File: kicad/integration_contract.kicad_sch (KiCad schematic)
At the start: 0 parts

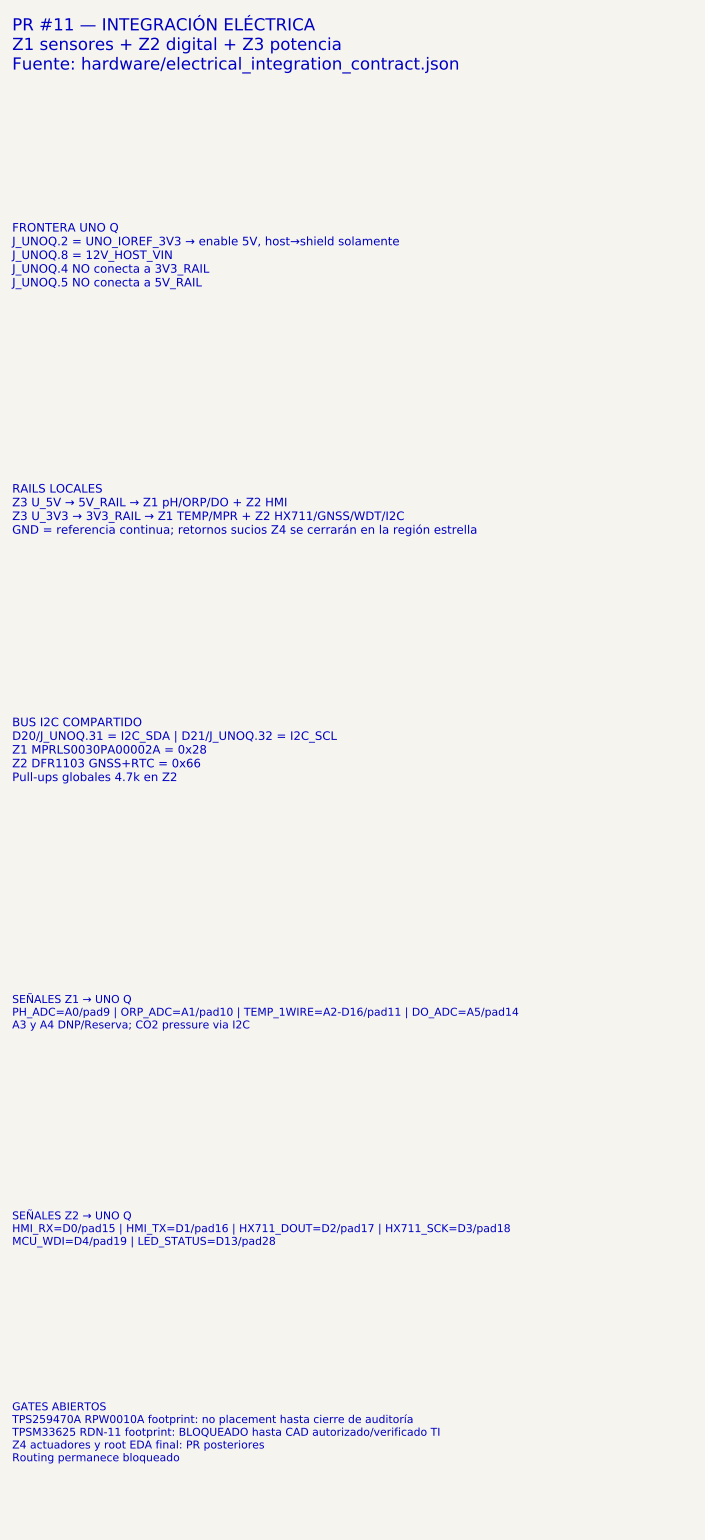
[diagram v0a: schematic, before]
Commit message: actuadores: congelar Z4 protegido y diagnosticable para Insight (#12)
Sustituye etapas legacy por DRV8242H-Q1, TPS1HC120C-Q1 y PhotoMOS AQY212EHAX; añade telemetría de bomba en A4, diagnóstico común D10, SELV/no-mains para chiller y gates Z4 con 10/10 checks verdes.
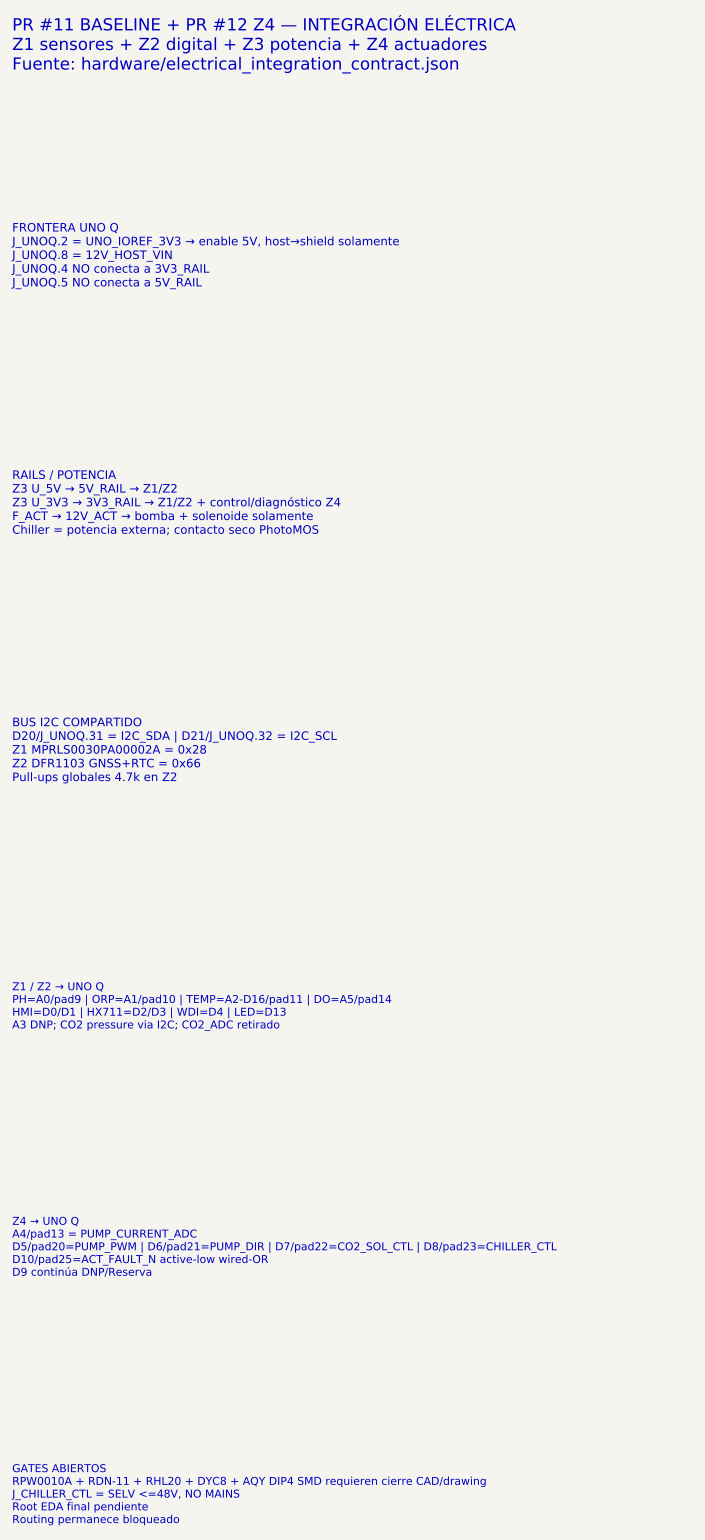
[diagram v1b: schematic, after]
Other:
- note added: "GATES ABIERTOS RPW0010A + RDN-11 + RHL20 + DYC8 + AQY DIP4 SMD requieren cierre CAD/drawing J_CHILLER_CTL = SELV <=48V, NO MAINS Root EDA final pendiente Routing permanece bloqueado"
- note added: "PR #11 BASELINE + PR #12 Z4 — INTEGRACIÓN ELÉCTRICA Z1 sensores + Z2 digital + Z3 potencia + Z4 actuadores Fuente: hardware/electrical_integration_contract.json"
- note added: "RAILS / POTENCIA Z3 U_5V → 5V_RAIL → Z1/Z2 Z3 U_3V3 → 3V3_RAIL → Z1/Z2 + control/diagnóstico Z4 F_ACT → 12V_ACT → bomba + solenoide solamente Chiller = potencia externa; contacto seco PhotoMOS"
- note added: "Z1 / Z2 → UNO Q PH=A0/pad9 | ORP=A1/pad10 | TEMP=A2-D16/pad11 | DO=A5/pad14 HMI=D0/D1 | HX711=D2/D3 | WDI=D4 | LED=D13 A3 DNP; CO2 pressure via I2C; CO2_ADC retirado"
- note added: "Z4 → UNO Q A4/pad13 = PUMP_CURRENT_ADC D5/pad20=PUMP_PWM | D6/pad21=PUMP_DIR | D7/pad22=CO2_SOL_CTL | D8/pad23=CHILLER_CTL D10/pad25=ACT_FAULT_N active-low wired-OR D9 continúa DNP/Reserva"
- note removed: "GATES ABIERTOS TPS259470A RPW0010A footprint: no placement hasta cierre de auditoría TPSM33625 RDN-11 footprint: BLOQUEADO hasta CAD autorizado/verificado TI Z4 actuadores y root EDA final: PR posteriores Routing permanece bloqueado"
- note removed: "PR #11 — INTEGRACIÓN ELÉCTRICA Z1 sensores + Z2 digital + Z3 potencia Fuente: hardware/electrical_integration_contract.json"
- note removed: "RAILS LOCALES Z3 U_5V → 5V_RAIL → Z1 pH/ORP/DO + Z2 HMI Z3 U_3V3 → 3V3_RAIL → Z1 TEMP/MPR + Z2 HX711/GNSS/WDT/I2C GND = referencia continua; retornos sucios Z4 se cerrarán en la región estrella"
- note removed: "SEÑALES Z1 → UNO Q PH_ADC=A0/pad9 | ORP_ADC=A1/pad10 | TEMP_1WIRE=A2-D16/pad11 | DO_ADC=A5/pad14 A3 y A4 DNP/Reserva; CO2 pressure via I2C"
- note removed: "SEÑALES Z2 → UNO Q HMI_RX=D0/pad15 | HMI_TX=D1/pad16 | HX711_DOUT=D2/pad17 | HX711_SCK=D3/pad18 MCU_WDI=D4/pad19 | LED_STATUS=D13/pad28"
- title: NFB Insight PCBA v2 — Integración eléctrica Z1 + Z2 + Potencia -> NFB Insight PCBA v2 — Integración eléctrica Z1 + Z2 + Z3 + Z4
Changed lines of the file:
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@@
 (kicad_sch
   (version 20250114)
-  (generator "nfb_pr11_integration_contract")
+  (generator "nfb_pr12_integration_contract")
   (generator_version "1.0")
   (paper "A3")
   (title_block
-    (title "NFB Insight PCBA v2 — Integración eléctrica Z1 + Z2 + Potencia")
+    (title "NFB Insight PCBA v2 — Integración eléctrica Z1 + Z2 + Z3 + Z4")
     (date "2026-08-12")
-    (rev "0.11.0")
+    (rev "0.12.0")
     (company "Cafelium SRL / Nebula Ecosystem")
-    (comment 1 "PR #11 — contrato de integración, no placement/routing")
+    (comment 1 "PR #11 baseline + extensión PR #12 Z4; no placement/routing")
     (comment 2 "Fuente de verdad: hardware/electrical_integration_contract.json")
-    (comment 3 "Z4 actuadores queda fuera de alcance")
-    (comment 4 "Footprints críticos abiertos bloquean placement de potencia")
+    (comment 3 "Z4 actuadores integrado contractualmente")
+    (comment 4 "Footprints críticos abiertos bloquean placement")
   )
-  (text "PR #11 — INTEGRACIÓN ELÉCTRICA\nZ1 sensores + Z2 digital + Z3 potencia\nFuente: hardware/electrical_integration_contract.json"
+  (text "PR #11 BASELINE + PR #12 Z4 — INTEGRACIÓN ELÉCTRICA\nZ1 sensores + Z2 digital + Z3 potencia + Z4 actuadores\nFuente: hardware/electrical_integration_contract.json"
     (exclude_from_sim no)
     (at 30.48 30.48 0)
@@
     (effects (font (size 1.4 1.4)) (justify left bottom))
   )
-  (text "RAILS LOCALES\nZ3 U_5V → 5V_RAIL → Z1 pH/ORP/DO + Z2 HMI\nZ3 U_3V3 → 3V3_RAIL → Z1 TEMP/MPR + Z2 HX711/GNSS/WDT/I2C\nGND = referencia continua; retornos sucios Z4 se cerrarán en la región estrella"
+  (text "RAILS / POTENCIA\nZ3 U_5V → 5V_RAIL → Z1/Z2\nZ3 U_3V3 → 3V3_RAIL → Z1/Z2 + control/diagnóstico Z4\nF_ACT → 12V_ACT → bomba + solenoide solamente\nChiller = potencia externa; contacto seco PhotoMOS"
     (exclude_from_sim no)
     (at 30.48 106.68 0)
@@
     (effects (font (size 1.4 1.4)) (justify left bottom))
   )
-  (text "SEÑALES Z1 → UNO Q\nPH_ADC=A0/pad9 | ORP_ADC=A1/pad10 | TEMP_1WIRE=A2-D16/pad11 | DO_ADC=A5/pad14\nA3 y A4 DNP/Reserva; CO2 pressure via I2C"
+  (text "Z1 / Z2 → UNO Q\nPH=A0/pad9 | ORP=A1/pad10 | TEMP=A2-D16/pad11 | DO=A5/pad14\nHMI=D0/D1 | HX711=D2/D3 | WDI=D4 | LED=D13\nA3 DNP; CO2 pressure via I2C; CO2_ADC retirado"
     (exclude_from_sim no)
     (at 30.48 187.96 0)
     (effects (font (size 1.3 1.3)) (justify left bottom))
   )
-  (text "SEÑALES Z2 → UNO Q\nHMI_RX=D0/pad15 | HMI_TX=D1/pad16 | HX711_DOUT=D2/pad17 | HX711_SCK=D3/pad18\nMCU_WDI=D4/pad19 | LED_STATUS=D13/pad28"
+  (text "Z4 → UNO Q\nA4/pad13 = PUMP_CURRENT_ADC\nD5/pad20=PUMP_PWM | D6/pad21=PUMP_DIR | D7/pad22=CO2_SOL_CTL | D8/pad23=CHILLER_CTL\nD10/pad25=ACT_FAULT_N active-low wired-OR\nD9 continúa DNP/Reserva"
     (exclude_from_sim no)
-    (at 30.48 223.52 0)
+    (at 30.48 228.6 0)
     (effects (font (size 1.3 1.3)) (justify left bottom))
   )
-  (text "GATES ABIERTOS\nTPS259470A RPW0010A footprint: no placement hasta cierre de auditoría\nTPSM33625 RDN-11 footprint: BLOQUEADO hasta CAD autorizado/verificado TI\nZ4 actuadores y root EDA final: PR posteriores\nRouting permanece bloqueado"
+  (text "GATES ABIERTOS\nRPW0010A + RDN-11 + RHL20 + DYC8 + AQY DIP4 SMD requieren cierre CAD/drawing\nJ_CHILLER_CTL = SELV <=48V, NO MAINS\nRoot EDA final pendiente\nRouting permanece bloqueado"
     (exclude_from_sim no)
-    (at 30.48 259.08 0)
+    (at 30.48 269.24 0)
     (effects (font (size 1.3 1.3)) (justify left bottom))
   )
